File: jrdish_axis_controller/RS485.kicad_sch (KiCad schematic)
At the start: 0 parts

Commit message: Updates
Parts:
- added C21, C26: 100nF, PCM_JLCPCB:C_0402, symbol PCM_JLCPCB-Capacitors:0402,100nF
- added C22, C27: 10uF, PCM_JLCPCB:C_0402, symbol PCM_JLCPCB-Capacitors:0402,10uF
- added C23, C25, C28, C30, C31: 10nF, PCM_JLCPCB:C_0402, symbol PCM_JLCPCB-Capacitors:0402,10nF
- added C24, C29: 1uF, PCM_JLCPCB:C_0402, symbol PCM_JLCPCB-Capacitors:0402,1uF
- added CN3: KF2EDGR-2.54-4P, MyParts:CONN-TH_4P-P2.54_KF2EDGR-2.54-4P, symbol MyParts:KF2EDGR-2.54-4P
- added H3: 210S-1*2P L=11.6MMGold-plated black, MyParts:HDR-TH_2P-P2.54-V-M-1, symbol MyParts:210S-1*2PL=11.6MMGold-platedblack
- added L1, L2, L3, L4: BLM15EX331SN1D, MyParts:L0402, symbol MyParts:BLM15EX331SN1D
- added R15: 4.7kΩ, PCM_JLCPCB:R_0402, symbol PCM_JLCPCB-Resistors:0402,4.7kΩ
- added R16: 120Ω, PCM_JLCPCB:R_0805, symbol PCM_JLCPCB-Resistors:0805,120Ω
- added U2: ISOW1432BDFMR, MyParts:SOIC-20_L12.8-W7.5-P1.27-LS10.3-BL, symbol MyParts:ISOW1432BDFMR
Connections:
- new net: C23.1, C24.1, C25.1, L2.2, U2.9 (VDD)
- new net: C28.1, C29.1, C30.1, L3.1, U2.12 (VISOOUT), U2.13 (MODE)
- new net: C28.2, C29.2, C30.2, L4.1, U2.11 (GND2)
- new net: C21.1, C22.1, L1.2, R15.1, U2.1 (VIO)
- new net: H3.2, R16.2
- new net: C26.1, C27.1, L3.2, U2.16 (VISOIN)
- new net: R15.2, U2.8 (EN/FLT)
- new net 3.3V: L1.1, L2.1
- new net GND: C21.2, C22.2, C23.2, C24.2, C25.2, U2.10 (GND1), U2.6 (GNDIO)
- new net GND_RS485: C26.2, C27.2, C31.1, CN3.3, L4.2, U2.15 (GISOIN)
- new net RS485_CHASSIS: C31.2, CN3.4
- new net RS485_DE_MCU: U2.3 (DE), U2.5 (~{RE})
- new net RS485_RX: CN3.1, R16.1, U2.18 (Z), U2.19 (B)
- new net RS485_TX: CN3.2, H3.1, U2.17 (Y), U2.20 (A)
- new net USART1_RX_MCU: U2.4 (R)
- new net USART1_TX_MCU: U2.2 (D)
- no-connect marks 0 -> 2
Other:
- note added: "C23 and C28 need to be 1mm from their respecive pins."
- note added: "Caps near VIO"
- note added: "HF Noise Bleed"
- note added: "Isolated RS485"
- note added: "L1/L2/L3/L4 are 205mΩ 330Ω@100MHz 700mA ±25% 0402 Ferrite Beads"
- note added: "Note: RS485 Cable Shield connects to Earth gound at the host"
- note added: "RS485_CHASSIS connects directly to chassis"

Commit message: Passes ERC
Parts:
- added CN6: KF2EDGR-2.54-4P, MyParts:CONN-TH_4P-P2.54_KF2EDGR-2.54-4P, symbol MyParts:KF2EDGR-2.54-4P
- renumbered C22 to C18, C21 to C19, C27 to C20, C26 to C21, C25 to C22, C24 to C23, C23 to C24, C28 to C25, C29 to C26, C30 to C27, C31 to C28, H3 to H1, R16 to R17, R15 to R18
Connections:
- net RS485_CHASSIS: now also CN6.4
- net RS485_RX: now also H1.1, CN6.1; no longer R17.1
- net RS485_TX: now also R17.2, CN6.2; no longer H1.1
- net at H1.2: now also R17.1; no longer R17.2
- net GND_RS485 renamed RS485_GND
- net RS485_GND: now also CN6.3
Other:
- note added: "RS485 terminator, 2.54mm"
- note added: "RS485_CHASSIS"
- note added: "RS485_GND"
- note added: "RS485_RX"
- note added: "RS485_TX"
- moved on the sheet: C18, C19, C20, C21, C22, C23, C24, C25, C26, C27, C28, CN3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

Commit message: PCB layout in progress
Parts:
- removed C18, C20: 10uF, PCM_JLCPCB:C_0402, symbol PCM_JLCPCB-Capacitors:0402,10uF
- added C19, C21: 10uF, PCM_JLCPCB:C_0603, symbol PCM_JLCPCB-Capacitors:0603,10uF
- renumbered C19 to C20, C21 to C22, C22 to C23, C23 to C24, C24 to C25, C25 to C26, C26 to C27, C27 to C28, C28 to C29, CN6 to CN4, H1 to H2
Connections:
- net GND: now also C19.2
- net RS485_GND: now also C21.2
- net at C20.1, L1.2, R18.1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: now also C19.1
- net at C22.1, L3.2, U2.16 (VISOIN): now also C21.1
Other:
- company: (none) -> JRSeti

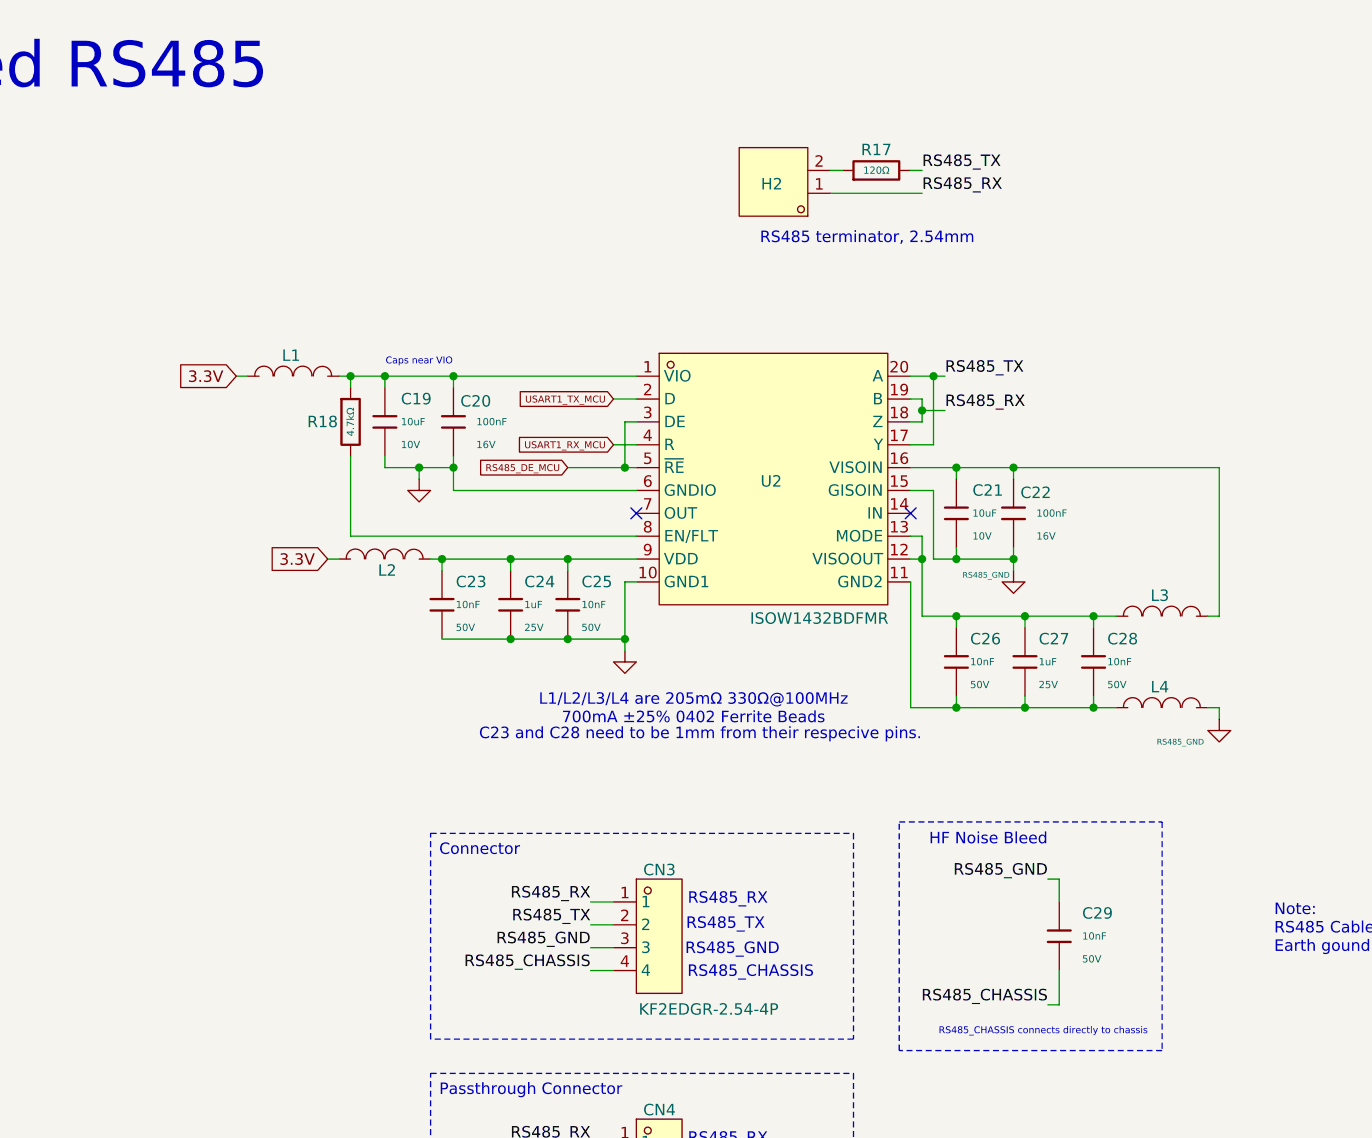
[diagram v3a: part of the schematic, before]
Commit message: New 64pin version - 2 axes
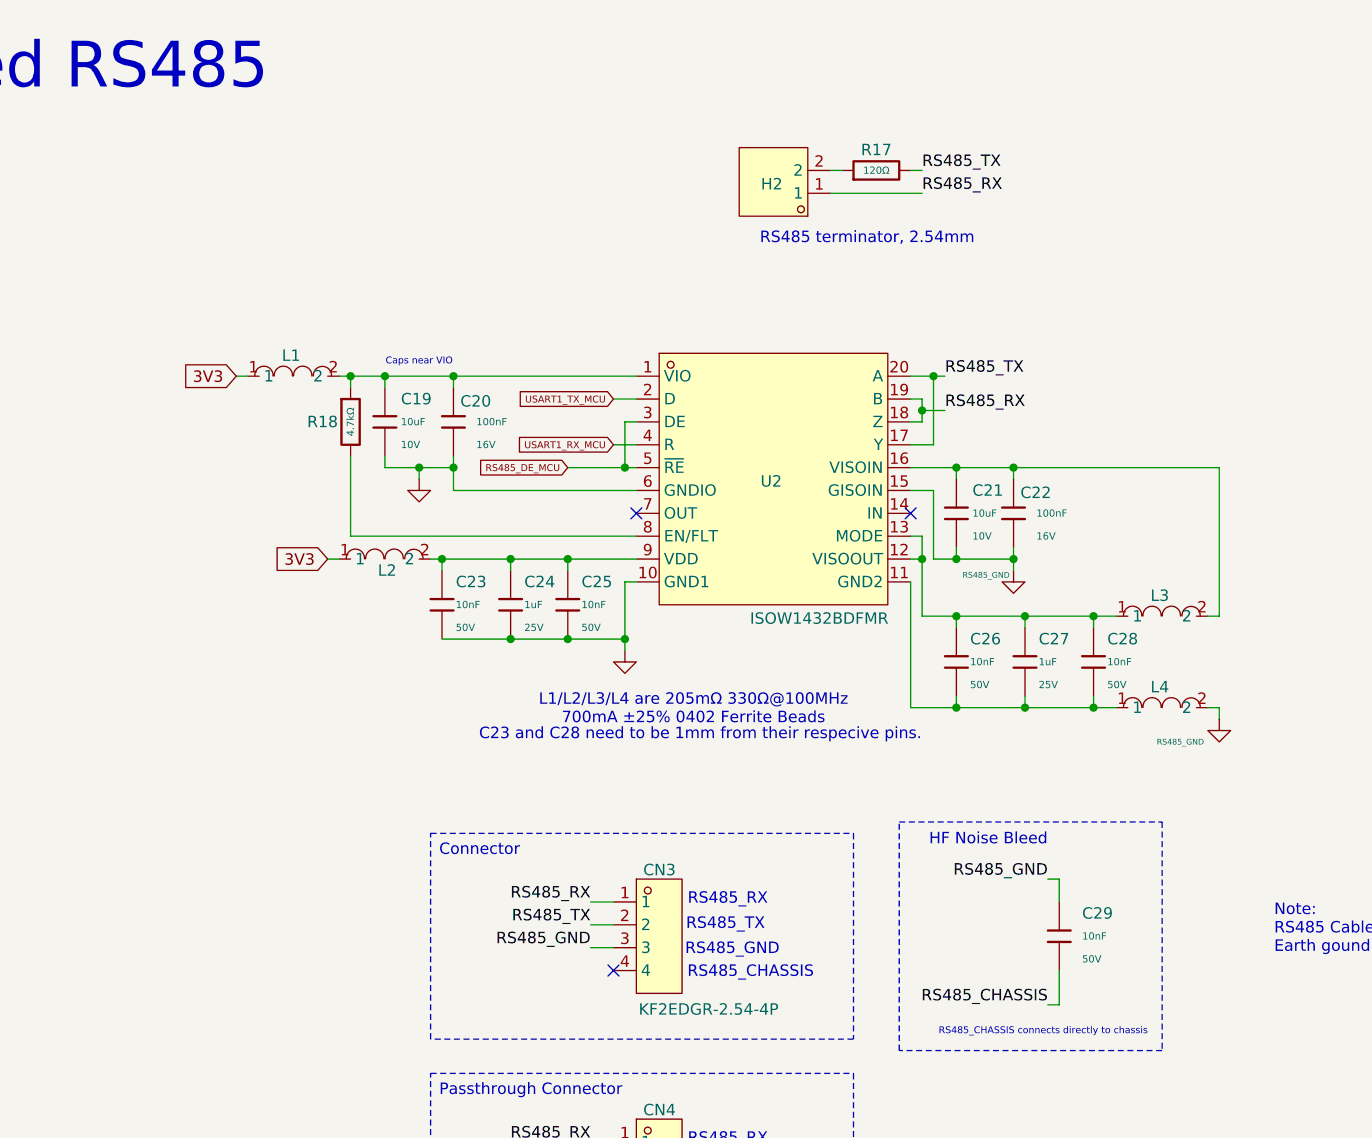
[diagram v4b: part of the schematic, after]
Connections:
- net RS485_CHASSIS: no longer CN3.4
- net 3.3V renamed 3V3
- no-connect marks 2 -> 3

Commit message: Continuing layout
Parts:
- added C22, C26: 10uF, PCM_JLCPCB:C_0603, symbol PCM_JLCPCB-Capacitors:0603,10uF
- added C23, C27: 100nF, PCM_JLCPCB:C_0402, symbol PCM_JLCPCB-Capacitors:0402,100nF
- added C31, C33, C37, C39: 10nF, PCM_JLCPCB:C_0402, symbol PCM_JLCPCB-Capacitors:0402,10nF
- added C32, C38: 1uF, PCM_JLCPCB:C_0402, symbol PCM_JLCPCB-Capacitors:0402,1uF
- added CN9: KF2EDGR-2.54-4P, MyParts:CONN-TH_4P-P2.54_KF2EDGR-2.54-4P, symbol MyParts:KF2EDGR-2.54-4P
- added L2, L4, L6, L8: BLM15EX331SN1D, MyParts:L0402, symbol MyParts:BLM15EX331SN1D
- added R19: 4.7kΩ, PCM_JLCPCB:R_0402, symbol PCM_JLCPCB-Resistors:0402,4.7kΩ
- added U3: ISOW1432BDFMR, MyParts:SOIC-20_L12.8-W7.5-P1.27-LS10.3-BL, symbol MyParts:ISOW1432BDFMR
- renumbered C19 to C20, C20 to C21, C21 to C24, C22 to C25, C23 to C28, C24 to C29, C25 to C30, C26 to C34, C27 to C35, C28 to C36, C29 to C40, CN4 to CN10, CN3 to CN11, L2 to L3, L3 to L5, L4 to L7
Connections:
- net 3V3: now also L2.1, L4.1
- net GND: now also L7.2, C22.2, C23.2, C31.2, C32.2, C33.2, U3.10 (GND1), U3.6 (GNDIO)
- net RS485_GND: now also C26.2, C27.2, CN9.3, L8.2, U3.15 (GISOIN); no longer L7.2
- net RS485_DE_MCU renamed RS485_1_DE_MCU
- net RS485_RX renamed RS485_1_RX
- net RS485_1_RX: now also CN10.2, CN11.2; no longer CN10.1, CN11.1
- net RS485_TX renamed RS485_1_TX
- net RS485_1_TX: now also CN10.1, CN11.1; no longer CN10.2, CN11.2
- net USART1_RX_MCU renamed RS485_1_RX_MCU
- net USART1_TX_MCU renamed RS485_1_TX_MCU
- new net: C37.1, C38.1, C39.1, L6.1, U3.12 (VISOOUT), U3.13 (MODE)
- new net: C26.1, C27.1, L6.2, U3.16 (VISOIN)
- new net: C22.1, C23.1, L2.2, R19.1, U3.1 (VIO)
- new net: C31.1, C32.1, C33.1, L4.2, U3.9 (VDD)
- new net: C37.2, C38.2, C39.2, L8.1, U3.11 (GND2)
- new net: R19.2, U3.8 (EN/FLT)
- new net RS485_2_DE_MCU: U3.3 (DE), U3.5 (~{RE})
- new net RS485_2_RX: CN9.2, U3.18 (Z), U3.19 (B)
- new net RS485_2_RX_MCU: U3.4 (R)
- new net RS485_2_TX: CN9.1, U3.17 (Y), U3.20 (A)
- new net RS485_2_TX_MCU: U3.2 (D)
- no-connect marks 3 -> 6
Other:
- note added: "RS485_1 To Host"
- note added: "RS485_1_RX"
- note added: "RS485_1_TX"
- note added: "RS485_2 Lead"
- note added: "RS485_2_RX"
- note added: "RS485_2_TX"
- note added: "There are 2 RS485 interfaces. 1 - To the Host computer, where the MCU is the follower. 2 - The MCU is an RS485 lead, able to send commands to other followers such as a servo driver."
- note removed: "RS485_RX"
- note removed: "RS485_TX"
- moved on the sheet: C20, C21, C24, C25, C28, C29, C30, C34, C35, C36, C40, CN10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

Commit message: Continuing layout
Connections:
- net GND: no longer L7.2
- net RS485_GND: now also L7.2
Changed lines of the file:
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@@
 		(in_pos_files yes)
 		(dnp no)
-		(fields_autoplaced yes)
 		(property "Reference" "#PWR028"
 			(at 139.7 90.17 0)
@@
 			)
 		)
-		(property "Value" "GND"
-			(at 139.7 88.9 0)
-			(hide yes)
+		(property "Value" "RS485_GND"
+			(at 139.192 87.884 0)
 			(show_name no)
 			(do_not_autoplace no)
